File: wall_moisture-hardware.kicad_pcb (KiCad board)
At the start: 4 copper layers, 78.4 x 99.3 mm, 40 parts, among them J1 Conn_01x04_Socket, J2 Conn_01x04_Socket, J3 Conn_01x03_Pin, J4 Conn_01x03_Pin, J5 490107670612, Q3 BC847,215, Q4 BSS316N, SW1 DSHP08TSGET, SW2 FSMH, U2 STM32L432KCUx, U3 TPS7A20xxxDBV, U4 TPS7A20xxxDBV, U7 OPA388IDBV, U8 AD7747, Y1 ECS-.327-7-12RR-TR

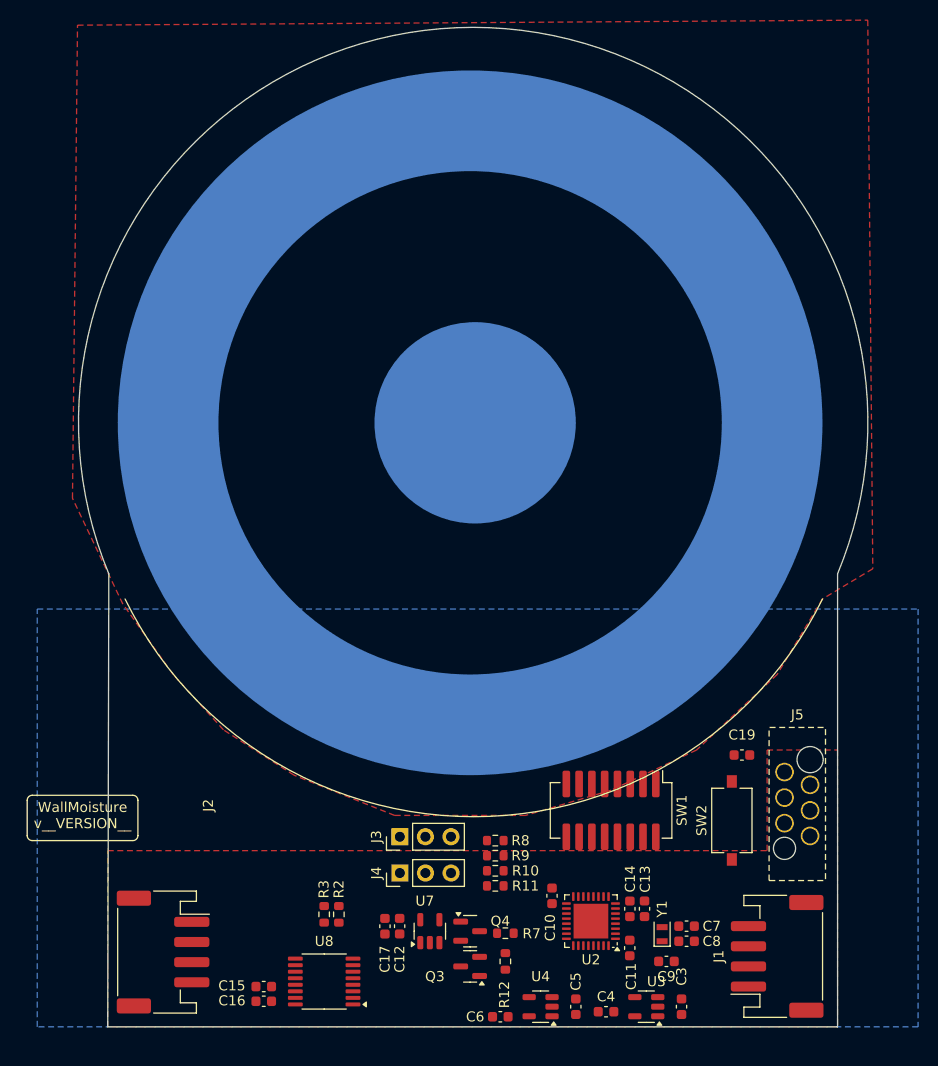
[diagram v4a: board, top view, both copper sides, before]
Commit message: design: complete the routing of the board
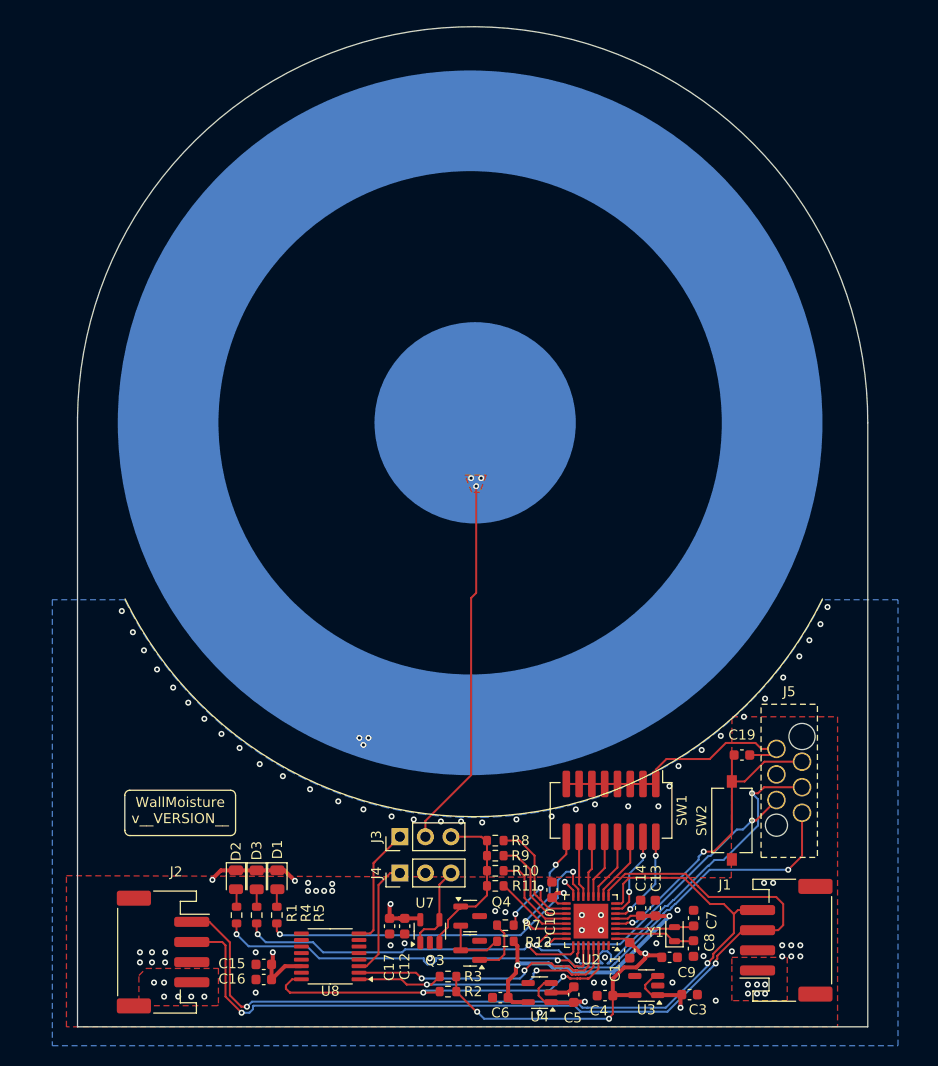
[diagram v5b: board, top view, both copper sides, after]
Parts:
- added D1: KT-0805B Blue, LED_SMD:LED_0805_2012Metric, F.Cu at (380.9, 95.4)
- added D2: KT-0805R Red, LED_SMD:LED_0805_2012Metric, F.Cu at (376.7, 95.4)
- added D3: KT-0805G Green, LED_SMD:LED_0805_2012Metric, F.Cu at (378.8, 95.4)
- added R1: 100, Resistor_SMD:R_0603_1608Metric, F.Cu at (376.8, 98.9)
- added R4: 100, Resistor_SMD:R_0603_1608Metric, F.Cu at (378.8, 98.9)
- added R5: 15, Resistor_SMD:R_0603_1608Metric, F.Cu at (380.8, 98.9)
- moved R3 13.8 mm to (397.8, 105.0), turned to 180 degrees
- moved R2 13.3 mm to (397.8, 106.5), turned to 180 degrees
- moved U8 2.57 mm to (386.1, 103.0)
- moved J5 2.44 mm to (431.7, 86.2)
- moved C15 2.20 mm to (379.5, 103.8)
- moved C16 2.16 mm to (379.5, 105.3)
- moved U3 2.10 mm to (417.5, 105.9)
- moved R12 2.00 mm to (403.5, 101.5), turned to 180 degrees
- moved C6 1.90 mm to (403.0, 107.1)
- moved J1 1.84 mm to (431.4, 101.4)
- moved C4 1.60 mm to (413.4, 106.9)
- moved Q3 1.60 mm to (400.0, 102.4)
- moved Q4 1.50 mm to (400.0, 99.0)
- moved C3 1.44 mm to (421.8, 106.8), turned to 0 degrees
- moved U4 1.40 mm to (406.9, 106.6)
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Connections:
- net /Analog frontend/SENSOR_EXC renamed /Analog frontend/SENSOR_EXC_MCU
- J3 pad 2: Net-(E1-+) -> /Analog frontend/SENSOR_EXCITATION
- U2 pad 15: /µC and digital/AN_IN -> /µC and digital/LED_B
- U2 pad 25: /µC and digital/JTDI -> /µC and digital/LED_G
- U2 pad 27: unconnected-(U2-PB4-Pad27) -> /µC and digital/LED_R
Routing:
- net /Connector and Power/MASTER_TX: track 0.00 -> 91.4 mm, vias 0 -> 2
- net /Connector and Power/MASTER_RX: track 0.00 -> 84.2 mm, vias 0 -> 2
- net GND: track 0.00 -> 55.8 mm, vias 0 -> 47
- net /Analog frontend/3.3V_LN: track 0.00 -> 42.8 mm, vias 0 -> 4
- net /µC and digital/SWDIO/JTMS: track 0.00 -> 39.7 mm, vias 0 -> 2
- net /µC and digital/LED_R: track 0.00 -> 39.7 mm, vias 0 -> 2
- net /µC and digital/I2C1_SDA: track 0.00 -> 38.9 mm, vias 0 -> 2
- net /µC and digital/TRACE/SWO/TDO: track 0.00 -> 37.0 mm, vias 0 -> 2
- net /Analog frontend/SENSOR_EXCITATION: track 0.00 -> 36.8 mm, vias 0 -> 3
- net /Connector and Power/3.3V: track 0.00 -> 36.7 mm, vias 0 -> 4
- net /µC and digital/LED_B: track 0.00 -> 36.7 mm, vias 0 -> 2
- net /µC and digital/LED_G: track 0.00 -> 34.7 mm, vias 0 -> 2
- net /µC and digital/NRST: track 0.00 -> 31.6 mm, vias 0 -> 2
- net /µC and digital/SWCLK/JTCK: track 0.00 -> 30.8 mm, vias 0 -> 2
- net /µC and digital/I2C1_SCL: track 0.00 -> 28.5 mm, vias 0 -> 2
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- added copper zone on F.Cu, net +5V
- added copper zone on In1.Cu, net +5V
- added copper zone on In1.Cu, net /Analog frontend/3.3V_LN
- added copper zone on F.Cu, net /Analog frontend/SENSOR_EXCITATION
- added copper zone on In2.Cu, net /Analog frontend/SENSOR_SHIELD
- added copper zone on In1.Cu, net /Connector and Power/3.3V
- added copper zone on In2.Cu, net GND
- removed copper zone on F.Cu, net /Analog frontend/SENSOR_SHIELD
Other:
- board size 78.4 x 99.3 mm -> 78.5 x 99.3 mm

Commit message: chore: fix the naming of connectors sheet file name and the change the path of footprints
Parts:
- C10, C11, C12, C13, C14, C15, C16, C17, C19, C3, C4, C5, C6, C7, C8, C9: footprint Capacitor_SMD:C_0603_1608Metric -> footprints:C_0603_1608Metric
- D1, D2, D3: footprint LED_SMD:LED_0805_2012Metric -> footprints:LED_0805_2012Metric
- E1: footprint el-ce:CapacitiveElectrode-round_20mmx70mm -> footprints:CapacitiveElectrode-round_20mmx70mm
- J1, J2: footprint Connector_JST:JST_PH_S4B-PH-SM4-TB_1x04-1MP_P2.00mm_Horizontal -> footprints:JST_PH_S4B-PH-SM4-TB_1x04-1MP_P2.00mm_Horizontal
- J3, J4: footprint Connector_PinHeader_2.54mm:PinHeader_1x03_P2.54mm_Vertical -> footprints:PinHeader_1x03_P2.54mm_Vertical
- J5: footprint el-ce:Skedd490107670612_2x06_P2.54mm_Debug -> footprints:Skedd490107670612_2x06_P2.54mm_Debug
- Q3, Q4: footprint Package_TO_SOT_SMD:SOT-23 -> footprints:SOT-23
- R1, R10, R11, R12, R2, R3, R4, R5, R7, R8, R9: footprint Resistor_SMD:R_0603_1608Metric -> footprints:R_0603_1608Metric
- SW1: footprint Button_Switch_SMD:SW_DIP_SPSTx08_Slide_KingTek_DSHP08TJ_W5.25mm_P1.27mm_JPin -> footprints:SW_DIP_SPSTx08_Slide_KingTek_DSHP08TJ_W5.25mm_P1.27mm_JPin
- SW2: footprint Button_Switch_SMD:SW_Tactile_SPST_NO_Straight_CK_PTS636Sx25SMTRLFS -> footprints:SW_Tactile_SPST_NO_Straight_CK_PTS636Sx25SMTRLFS
- U2: footprint Package_DFN_QFN:QFN-32-1EP_5x5mm_P0.5mm_EP3.45x3.45mm -> footprints:QFN-32-1EP_5x5mm_P0.5mm_EP3.45x3.45mm
- U3, U4, U7: footprint Package_TO_SOT_SMD:SOT-23-5 -> footprints:SOT-23-5
- U8: footprint Package_SO:TSSOP-16_4.4x5mm_P0.65mm -> footprints:TSSOP-16_4.4x5mm_P0.65mm
- Y1: footprint Crystal:Crystal_SMD_2012-2Pin_2.0x1.2mm -> footprints:Crystal_SMD_2012-2Pin_2.0x1.2mm
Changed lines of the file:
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@@
 	(net 50 "/µC and digital/LED_G")
 	(net 51 "/µC and digital/LED_B")
-	(footprint "Connector_PinHeader_2.54mm:PinHeader_1x03_P2.54mm_Vertical"
+	(footprint "footprints:PinHeader_1x03_P2.54mm_Vertical"
 		(layer "F.Cu")
 		(at 393.01779 91.116836 90)
@@
 		)
 	)
-	(footprint "Capacitor_SMD:C_0603_1608Metric"
+	(footprint "footprints:C_0603_1608Metric"
 		(layer "F.Cu")
 		(at 419.812538 103.095402)
@@
 		)
 	)
-	(footprint "Resistor_SMD:R_0603_1608Metric"
+	(footprint "footprints:R_0603_1608Metric"
 		(layer "F.Cu")
 		(at 376.799 98.9 -90)
@@
 		)
 	)
-	(footprint "Resistor_SMD:R_0603_1608Metric"
+	(footprint "footprints:R_0603_1608Metric"
 		(layer "F.Cu")
 		(at 403.5 101.5 180)
@@
 		)
 	)
-	(footprint "Crystal:Crystal_SMD_2012-2Pin_2.0x1.2mm"
+	(footprint "footprints:Crystal_SMD_2012-2Pin_2.0x1.2mm"
 		(layer "F.Cu")
 		(at 420.3 100.79772 90)
@@
 		)
 	)
-	(footprint "Resistor_SMD:R_0603_1608Metric"
+	(footprint "footprints:R_0603_1608Metric"
 		(layer "F.Cu")
 		(at 402.5 93 180)
@@
 		)
 	)
-	(footprint "Package_TO_SOT_SMD:SOT-23"
+	(footprint "footprints:SOT-23"
 		(layer "F.Cu")
 		(at 400 102.4 180)
@@
 		)
 	)
-	(footprint "Package_SO:TSSOP-16_4.4x5mm_P0.65mm"
+	(footprint "footprints:TSSOP-16_4.4x5mm_P0.65mm"
 		(layer "F.Cu")
 		(at 386.1 103 180)
@@
 		)
 	)
-	(footprint "Capacitor_SMD:C_0603_1608Metric"
+	(footprint "footprints:C_0603_1608Metric"
 		(layer "F.Cu")
 		(at 422.185819 102.223709 90)
@@
 		)
 	)
-	(footprint "Connector_JST:JST_PH_S4B-PH-SM4-TB_1x04-1MP_P2.00mm_Horizontal"
+	(footprint "footprints:JST_PH_S4B-PH-SM4-TB_1x04-1MP_P2.00mm_Horizontal"
 		(layer "F.Cu")
 		(at 431.4 101.4 90)
@@
 		)
 	)
-	(footprint "Capacitor_SMD:C_0603_1608Metric"
+	(footprint "footprints:C_0603_1608Metric"
 		(layer "F.Cu")
 		(at 413.4 106.9 180)
@@
 		)
 	)
-	(footprint "Capacitor_SMD:C_0603_1608Metric"
+	(footprint "footprints:C_0603_1608Metric"
 		(layer "F.Cu")
 		(at 427 83 180)
@@
 		)
 	)
-	(footprint "Resistor_SMD:R_0603_1608Metric"
+	(footprint "footprints:R_0603_1608Metric"
 		(layer "F.Cu")
 		(at 402.5 91.5 180)
@@
 		)
 	)
-	(footprint "Capacitor_SMD:C_0603_1608Metric"
+	(footprint "footprints:C_0603_1608Metric"
 		(layer "F.Cu")
 		(at 418.4 98.2 90)
@@
 		)
 	)
-	(footprint "Capacitor_SMD:C_0603_1608Metric"
+	(footprint "footprints:C_0603_1608Metric"
 		(layer "F.Cu")
 		(at 392 100 -90)
@@
 		)
 	)
-	(footprint "Package_TO_SOT_SMD:SOT-23"
+	(footprint "footprints:SOT-23"
 		(layer "F.Cu")
 		(at 400 99)
@@
 		)
 	)
-	(footprint "Package_TO_SOT_SMD:SOT-23-5"
+	(footprint "footprints:SOT-23-5"
 		(layer "F.Cu")
 		(at 417.5 105.9 180)
@@
 		)
 	)
-	(footprint "Package_DFN_QFN:QFN-32-1EP_5x5mm_P0.5mm_EP3.45x3.45mm"
+	(footprint "footprints:QFN-32-1EP_5x5mm_P0.5mm_EP3.45x3.45mm"
 		(layer "F.Cu")
 		(at 412 99.5 180)
@@
 		)
 	)
-	(footprint "Resistor_SMD:R_0603_1608Metric"
+	(footprint "footprints:R_0603_1608Metric"
 		(layer "F.Cu")
 		(at 397.8 105 180)
@@
 		)
 	)
-	(footprint "Resistor_SMD:R_0603_1608Metric"
+	(footprint "footprints:R_0603_1608Metric"
 		(layer "F.Cu")
 		(at 402.5 96 180)
@@
 		)
 	)
-	(footprint "LED_SMD:LED_0805_2012Metric"
+	(footprint "footprints:LED_0805_2012Metric"
 		(layer "F.Cu")
 		(at 380.85157 95.39148 -90)
@@
 		)
 	)
-	(footprint "LED_SMD:LED_0805_2012Metric"
+	(footprint "footprints:LED_0805_2012Metric"
 		(layer "F.Cu")
 		(at 378.799 95.4 -90)
@@
 		)
 	)
-	(footprint "Button_Switch_SMD:SW_Tactile_SPST_NO_Straight_CK_PTS636Sx25SMTRLFS"
+	(footprint "footprints:SW_Tactile_SPST_NO_Straight_CK_PTS636Sx25SMTRLFS"
 		(layer "F.Cu")
 		(at 426 89.5 90)
@@
 		)
 	)
-	(footprint "LED_SMD:LED_0805_2012Metric"
+	(footprint "footprints:LED_0805_2012Metric"
 		(layer "F.Cu")
 		(at 376.742543 95.385936 -90)
@@
 		)
 	)
-	(footprint "Resistor_SMD:R_0603_1608Metric"
+	(footprint "footprints:R_0603_1608Metric"
 		(layer "F.Cu")
 		(at 397.8 106.5 180)
@@
 		)
 	)
-	(footprint "Capacitor_SMD:C_0603_1608Metric"
+	(footprint "footprints:C_0603_1608Metric"
 		(layer "F.Cu")
 		(at 410.3 106.8 90)
@@
 		)
 	)
-	(footprint "Capacitor_SMD:C_0603_1608Metric"
+	(footprint "footprints:C_0603_1608Metric"
 		(layer "F.Cu")
 		(at 403 107.1 180)
@@
 		)
 	)
-	(footprint "Resistor_SMD:R_0603_1608Metric"
+	(footprint "footprints:R_0603_1608Metric"
 		(layer "F.Cu")
 		(at 378.799 98.9 -90)
@@
 		)
 	)
-	(footprint "Capacitor_SMD:C_0603_1608Metric"
+	(footprint "footprints:C_0603_1608Metric"
 		(layer "F.Cu")
 		(at 379.5 105.3 180)
@@
 		)
 	)
-	(footprint "Capacitor_SMD:C_0603_1608Metric"
+	(footprint "footprints:C_0603_1608Metric"
 		(layer "F.Cu")
 		(at 415.856289 102.4 -90)
@@
 		)
 	)
-	(footprint "Connector_JST:JST_PH_S4B-PH-SM4-TB_1x04-1MP_P2.00mm_Horizontal"
+	(footprint "footprints:JST_PH_S4B-PH-SM4-TB_1x04-1MP_P2.00mm_Horizontal"
 		(layer "F.Cu")
 		(at 369.5 102.573485 -90)
@@
 		)
 	)
-	(footprint "Package_TO_SOT_SMD:SOT-23-5"
+	(footprint "footprints:SOT-23-5"
 		(layer "F.Cu")
 		(at 406.9 106.6 180)
@@
 		)
 	)
-	(footprint "Button_Switch_SMD:SW_DIP_SPSTx08_Slide_KingTek_DSHP08TJ_W5.25mm_P1.27mm_JPin"
+	(footprint "footprints:SW_DIP_SPSTx08_Slide_KingTek_DSHP08TJ_W5.25mm_P1.27mm_JPin"
 		(layer "F.Cu")
 		(at 414 88.5 -90)
@@
 		)
 	)
-	(footprint "Resistor_SMD:R_0603_1608Metric"
+	(footprint "footprints:R_0603_1608Metric"
 		(layer "F.Cu")
 		(at 403.5 99.9 180)
@@
 		)
 	)
-	(footprint "Resistor_SMD:R_0603_1608Metric"
+	(footprint "footprints:R_0603_1608Metric"
 		(layer "F.Cu")
 		(at 380.799 98.9 90)
@@
 		)
 	)
-	(footprint "Resistor_SMD:R_0603_1608Metric"
+	(footprint "footprints:R_0603_1608Metric"
 		(layer "F.Cu")
 		(at 402.5 94.5 180)
@@
 		)
 	)
-	(footprint "Capacitor_SMD:C_0603_1608Metric"
+	(footprint "footprints:C_0603_1608Metric"
 		(layer "F.Cu")
 		(at 416.936037 98.193343 90)
@@
 		)
 	)
-	(footprint "Capacitor_SMD:C_0603_1608Metric"
+	(footprint "footprints:C_0603_1608Metric"
 		(layer "F.Cu")
 		(at 421.8 106.8)
@@
 		)
 	)
-	(footprint "Capacitor_SMD:C_0603_1608Metric"
+	(footprint "footprints:C_0603_1608Metric"
 		(layer "F.Cu")
 		(at 379.5 103.8 180)
@@
 		)
 	)
-	(footprint "Capacitor_SMD:C_0603_1608Metric"
+	(footprint "footprints:C_0603_1608Metric"
 		(layer "F.Cu")
 		(at 408.134364 96.4 90)
@@
 		)
 	)
-	(footprint "Capacitor_SMD:C_0603_1608Metric"
+	(footprint "footprints:C_0603_1608Metric"
 		(layer "F.Cu")
 		(at 393.5 100 -90)
@@
 		)
 	)
-	(footprint "el-ce:Skedd490107670612_2x06_P2.54mm_Debug"
+	(footprint "footprints:Skedd490107670612_2x06_P2.54mm_Debug"
 		(layer "F.Cu")
 		(at 431.7 86.2 90)
@@
 		)
 	)
-	(footprint "Package_TO_SOT_SMD:SOT-23-5"
+	(footprint "footprints:SOT-23-5"
 		(layer "F.Cu")
 		(at 396 100.5 90)
@@
 		)
 	)
-	(footprint "Capacitor_SMD:C_0603_1608Metric"
+	(footprint "footprints:C_0603_1608Metric"
 		(layer "F.Cu")
 		(at 422.2 99.2 -90)
@@
 		)
 	)
-	(footprint "Connector_PinHeader_2.54mm:PinHeader_1x03_P2.54mm_Vertical"
+	(footprint "footprints:PinHeader_1x03_P2.54mm_Vertical"
 		(layer "F.Cu")
 		(at 393.022812 94.72079 90)
@@
 		)
 	)
-	(footprint "el-ce:CapacitiveElectrode-round_20mmx70mm"
+	(footprint "footprints:CapacitiveElectrode-round_20mmx70mm"
 		(layer "B.Cu")
 		(at 400 50)
